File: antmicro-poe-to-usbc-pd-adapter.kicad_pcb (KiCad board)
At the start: 2 copper layers, 17 parts, among them J1 Bus_RJ45_5-2337992-8, J2 Bus_RJ45_5-2337992-8, J3 USB-C_WE_632723300011, U1 TPS2372-3RGWR, U2 LV14540DDAR, U3 STUSB4710AQ1TR, U4 IEA48003A280V-001-R

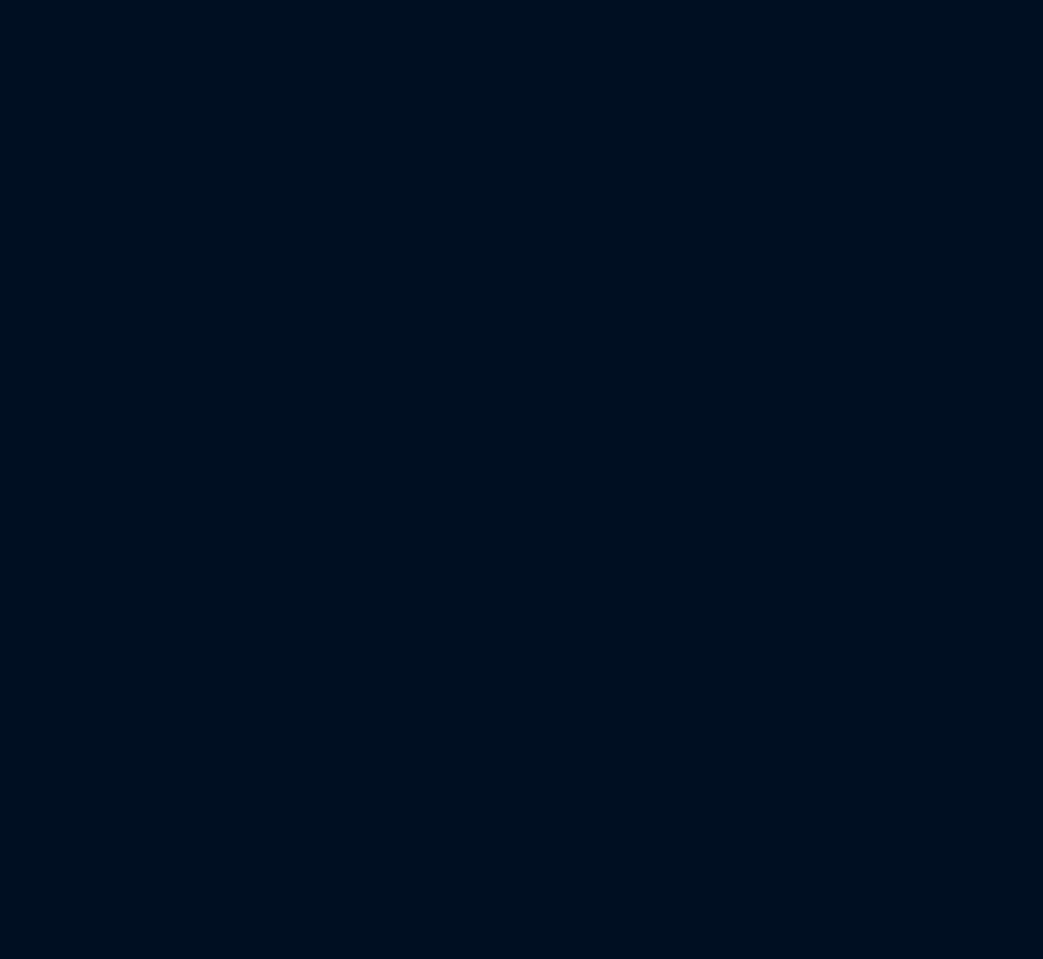
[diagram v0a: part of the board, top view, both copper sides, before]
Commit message: [#62182] Major changes in schematic
Add TPS65987D
Add FT4232H
Add 3v3 buck
Connect components
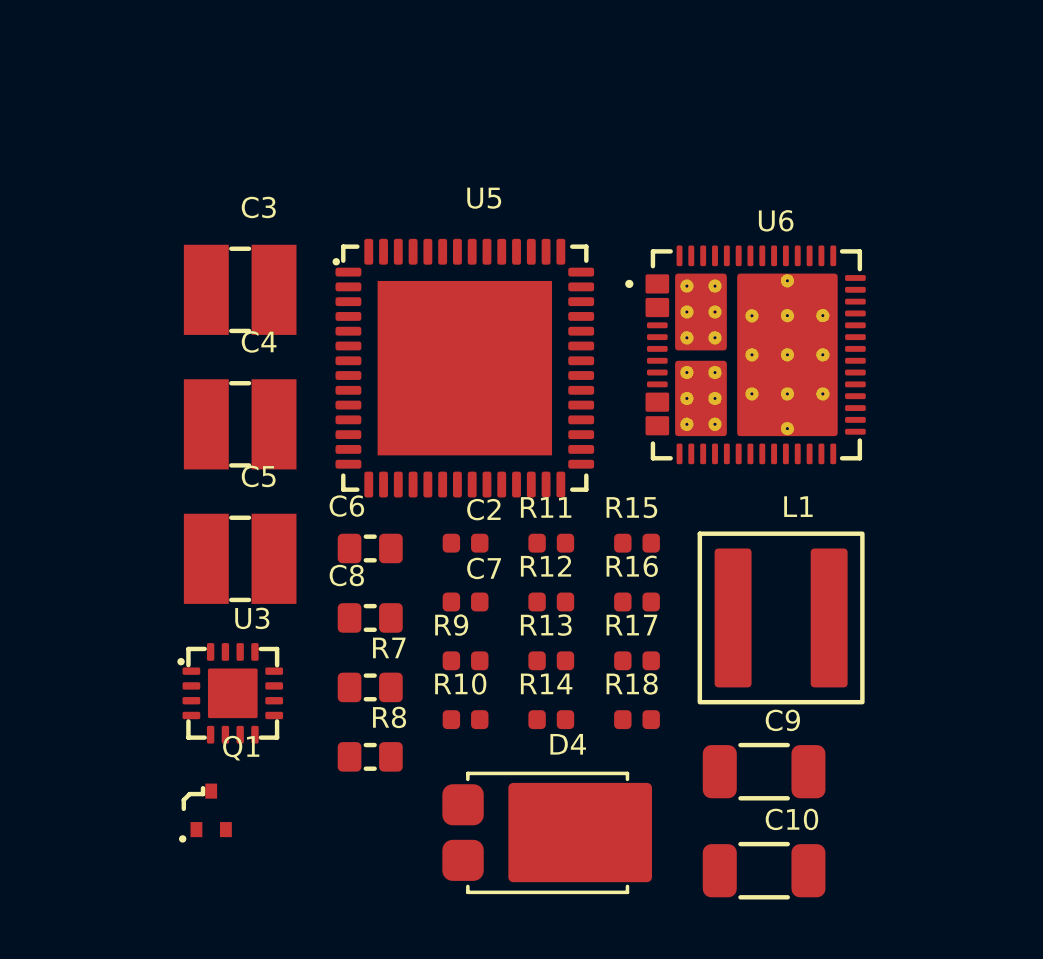
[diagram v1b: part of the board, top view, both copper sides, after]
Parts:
- added C10: C_47u_25V_1206, antmicro-footprints:C_1206_3216Metric, F.Cu at (149.1, 142.7)
- added C2: C_10n_50V_X7R_0402, antmicro-footprints:C_0402_1005Metric, F.Cu at (139.0, 131.6)
- added C3: C_4u7_1210_100V, antmicro-footprints:C_1210_3225Metric, F.Cu at (131.3, 123.1)
- added C4: C_2u2_1210, antmicro-footprints:C_1210_3225Metric, F.Cu at (131.3, 127.6)
- added C5: C_2u2_1210, antmicro-footprints:C_1210_3225Metric, F.Cu at (131.3, 132.2)
- added C6: C_100n_100V_X7R_0603, antmicro-footprints:C_0603_1608Metric, F.Cu at (135.7, 131.8)
- added C7: C_3n3_0402, antmicro-footprints:C_0402_1005Metric, F.Cu at (139.0, 133.6)
- added C8: C_100n_100V_X7R_0603, antmicro-footprints:C_0603_1608Metric, F.Cu at (135.7, 134.2)
- added C9: C_47u_25V_1206, antmicro-footprints:C_1206_3216Metric, F.Cu at (149.1, 139.4)
- added D4: PDS760, antmicro-footprints:PowerDI5, F.Cu at (141.7, 141.4)
- added L1: L_6u8_6.1A_MPS-MPL-AL5050, antmicro-footprints:L_MPS-MPL-AL5050, F.Cu at (149.6, 134.2)
- added Q1: PJE138K, antmicro-footprints:SOT-523, F.Cu at (130.4, 140.7)
- added R10: R_470k_0402, antmicro-footprints:R_0402_1005Metric, F.Cu at (139.0, 137.6)
- added R11: R_100k_0402, antmicro-footprints:R_0402_1005Metric, F.Cu at (141.9, 131.6)
- added R12: R_10k_0402, antmicro-footprints:R_0402_1005Metric, F.Cu at (141.9, 133.6)
- added R13: R_200k_0402, antmicro-footprints:R_0402_1005Metric, F.Cu at (141.9, 135.6)
- added R14: R_7k68_0402, antmicro-footprints:R_0402_1005Metric, F.Cu at (141.9, 137.6)
- added R15: R_2k7_0402, antmicro-footprints:R_0402_1005Metric, F.Cu at (144.8, 131.6)
- added R16: R_2k7_0402, antmicro-footprints:R_0402_1005Metric, F.Cu at (144.8, 133.6)
- added R17: R_4k7_0402, antmicro-footprints:R_0402_1005Metric, F.Cu at (144.8, 135.6)
- added R18: R_17k4_0402, antmicro-footprints:R_0402_1005Metric, F.Cu at (144.8, 137.6)
- added R7: R_0R_0603, antmicro-footprints:R_0603_1608Metric, F.Cu at (135.7, 136.5)
- added R8: R_0R_0603, antmicro-footprints:R_0603_1608Metric, F.Cu at (135.7, 138.9)
- added R9: R_27k_0402, antmicro-footprints:R_0402_1005Metric, F.Cu at (139.0, 135.6)
- added U3: INA230AIRGTR, antmicro-footprints:VQFN-16-1EP_3x3mm_P0.5mm_EP1.68x1.68mm, F.Cu at (131.1, 136.7)
- added U5: FT4232H_VQFN, antmicro-footprints:QFN-56-1EP_8x8mm_P0.5mm, F.Cu at (138.9, 125.7)
- added U6: TPS65988DHRSHR, antmicro-footprints:IC_TPS65987DDHRSHR, F.Cu at (148.8, 125.3)
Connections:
- U1 pad 11: unconnected-(U1-RTNA-Pad11) -> GNDD
- U1 pad 12: unconnected-(U1-RTNB-Pad12) -> GNDD
- U1 pad 13: unconnected-(U1-PG-Pad13) -> Net-(U1-PG)
- U2 pad 1: unconnected-(U2-BOOT-Pad1) -> Net-(U2-BOOT)
- U2 pad 2: unconnected-(U2-VIN-Pad2) -> Net-(U2-EN)
- U2 pad 3: unconnected-(U2-EN-Pad3) -> Net-(U2-EN)
- U2 pad 4: unconnected-(U2-RT-Pad4) -> Net-(U2-RT)
- U2 pad 5: unconnected-(U2-FB-Pad5) -> Net-(U2-FB)
- U2 pad 6: unconnected-(U2-SS-Pad6) -> Net-(U2-SS)
- U2 pad 7: Net-(U2-GND-Pad7) -> GND
- U2 pad 8: unconnected-(U2-SW-Pad8) -> Net-(D4-C)
- U2 pad 9: Net-(U2-GND-Pad7) -> GND
- U4 pad 1: unconnected-(U4-VIN+-Pad1) -> /VDD
- U4 pad 2: unconnected-(U4-!ON-Pad2) -> Net-(Q1-D)
- U4 pad 3: unconnected-(U4-VIN--Pad3) -> GNDD
- U4 pad 4: unconnected-(U4-VOUT--Pad4) -> GND
- U4 pad 5: unconnected-(U4-SENSE--Pad5) -> GND
- U4 pad 6: unconnected-(U4-TRIM-Pad6) -> Net-(U4-TRIM)
- U4 pad 7: unconnected-(U4-SENSE+-Pad7) -> Net-(U2-EN)
- U4 pad 8: unconnected-(U4-VOUT+-Pad8) -> Net-(U2-EN)
